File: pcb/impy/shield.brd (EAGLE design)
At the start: 133 x 107 mm, 117 parts, among them J1 USB-2410-06, J2 SI-60062-F, J3 5V, U1 AD5933YRS, U10 LTC3406AB, U11 23LCV1024-I/SN, U12 MIC2009A-1YM6, U13 ADG725BSU, U14 ADG725BSU, U2 ADG704BRM, U3 AD8656ARZ, U4 M24C08WMN, U5 ADG706BRU, U6 DP83848I, U7 MIC2009A-1YM6, U8 AT25DF081A-SS, U9 SST25VF080B-80-4I-S2

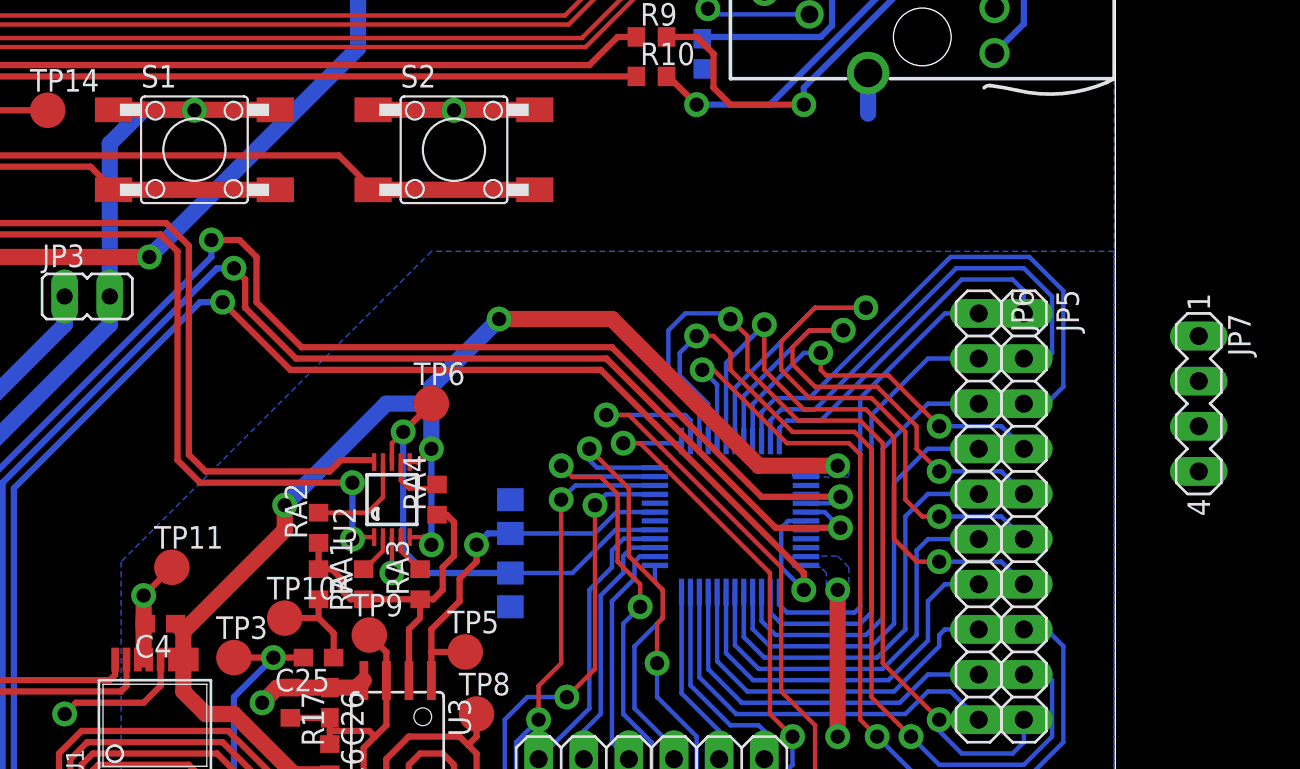
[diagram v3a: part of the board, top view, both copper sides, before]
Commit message: * pcb/impy: (shield.brd) Place and connect I2C header.
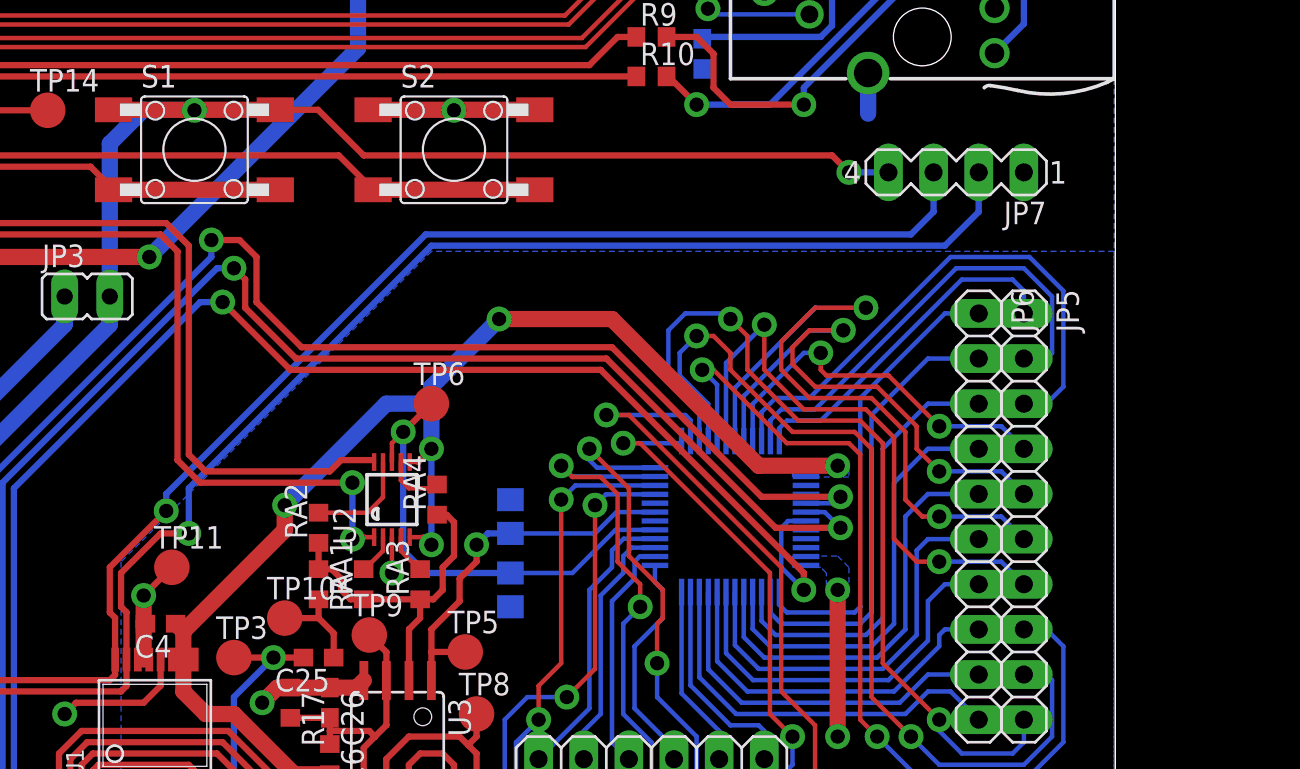
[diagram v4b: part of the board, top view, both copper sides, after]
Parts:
- moved JP7 18.9 mm to (86.0, 74.0), turned to 180 degrees
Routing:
- net PB9: track 27.5 -> 92.9 mm, vias 1 -> 2
- net PB6: track 29.6 -> 92.3 mm, vias 1 -> 2
- net VDD: track 58.3 -> 94.3 mm, vias 1 -> 2
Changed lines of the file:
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@@
 <attribute name="RS" value="737-8791" x="97.155" y="-6.35" size="1.778" layer="27" display="off"/>
 </element>
-<element name="JP7" library="con-lstb" package="MA04-1" value="I2C" x="99.695" y="60.96" rot="R270">
-<attribute name="OC_NEWARK" value="unknown" x="3.175" y="0" size="1.778" layer="27" rot="R270" display="off"/>
-<attribute name="MPN" value="" x="3.175" y="0" size="1.778" layer="27" rot="R270" display="off"/>
-<attribute name="MF" value="" x="3.175" y="0" size="1.778" layer="27" rot="R270" display="off"/>
-<attribute name="OC_FARNELL" value="unknown" x="3.175" y="0" size="1.778" layer="27" rot="R270" display="off"/>
+<element name="JP7" library="con-lstb" package="MA04-1" value="I2C" x="86.0425" y="73.9775" rot="R180">
+<attribute name="OC_NEWARK" value="unknown" x="25.0825" y="170.4975" size="1.778" layer="27" rot="R180" display="off"/>
+<attribute name="MPN" value="" x="25.0825" y="170.4975" size="1.778" layer="27" rot="R180" display="off"/>
+<attribute name="MF" value="" x="25.0825" y="170.4975" size="1.778" layer="27" rot="R180" display="off"/>
+<attribute name="OC_FARNELL" value="unknown" x="25.0825" y="170.4975" size="1.778" layer="27" rot="R180" display="off"/>
 </element>
 <element name="U6" library="parts" package="LQFP48" value="DP83848I" x="-10.795" y="78.105" rot="MR270">
@@
 <contactref element="JP7" pad="4"/>
 <wire x1="30.48" y1="57.4675" x2="38.4175" y2="65.405" width="0.9144" layer="16"/>
-<wire x1="47.73" y1="77.4975" x2="99.695" y2="57.15" width="0" layer="19" extent="1-1"/>
+<wire x1="47.73" y1="77.4975" x2="50.1375" y2="77.4975" width="0.3556" layer="1"/>
+<wire x1="50.1375" y1="77.4975" x2="52.705" y2="74.93" width="0.3556" layer="1"/>
+<wire x1="52.705" y1="74.93" x2="79.0575" y2="74.93" width="0.3556" layer="1"/>
+<wire x1="79.0575" y1="74.93" x2="80.01" y2="73.9775" width="0.3556" layer="1"/>
+<via x="80.01" y="73.9775" extent="1-16" drill="0.8" shape="octagon"/>
+<wire x1="80.01" y1="73.9775" x2="82.2325" y2="73.9775" width="0.3556" layer="16"/>
 <wire x1="-24.13" y1="60.96" x2="30.48" y2="57.4675" width="0" layer="19" extent="16-16"/>
 <wire x1="-26.67" y1="60.96" x2="-24.13" y2="60.96" width="0" layer="19" extent="1-1"/>
@@
 <wire x1="36.5125" y1="44.1325" x2="35.8775" y2="43.4975" width="0.3556" layer="1"/>
 <via x="35.8775" y="43.4975" extent="1-16" drill="0.8" shape="octagon"/>
-<wire x1="81.0895" y1="77.2795" x2="99.695" y2="64.77" width="0" layer="19" extent="16-16"/>
-<wire x1="-26.67" y1="58.42" x2="-26.67" y2="63.5" width="0" layer="19" extent="1-1"/>
-<wire x1="-26.67" y1="35.56" x2="-26.67" y2="58.42" width="0" layer="19" extent="1-1"/>
-<wire x1="-51.7525" y1="41.5325" x2="-26.67" y2="35.56" width="0" layer="19" extent="1-1"/>
-<wire x1="-57.4675" y1="44.5525" x2="-51.7525" y2="41.5325" width="0" layer="19" extent="1-1"/>
-<wire x1="-66.3575" y1="49.1525" x2="-57.4675" y2="44.5525" width="0" layer="19" extent="1-1"/>
-<wire x1="-67.6275" y1="49.1525" x2="-66.3575" y2="49.1525" width="0" layer="19" extent="1-1"/>
+<wire x1="-73.9775" y1="38.9925" x2="-79.6925" y2="41.3775" width="0" layer="19" extent="1-1"/>
+<wire x1="-73.9875" y1="38.4385" x2="-73.9775" y2="38.9925" width="0" layer="19" extent="1-1"/>
+<wire x1="-67.6275" y1="49.1525" x2="-73.9775" y2="38.9925" width="0" layer="19" extent="1-1"/>
+<wire x1="-66.3575" y1="49.1525" x2="-67.6275" y2="49.1525" width="0" layer="19" extent="1-1"/>
 <wire x1="-72.0725" y1="52.1725" x2="-67.6275" y2="49.1525" width="0" layer="19" extent="1-1"/>
 <wire x1="-68.8975" y1="54.3525" x2="-72.0725" y2="52.1725" width="0" layer="19" extent="1-1"/>
-<wire x1="-73.9775" y1="38.9925" x2="-67.6275" y2="49.1525" width="0" layer="19" extent="1-1"/>
-<wire x1="-73.9875" y1="38.4385" x2="-73.9775" y2="38.9925" width="0" layer="19" extent="1-1"/>
-<wire x1="-79.6925" y1="41.3775" x2="-73.9775" y2="38.9925" width="0" layer="19" extent="1-1"/>
+<wire x1="-57.4675" y1="44.5525" x2="-66.3575" y2="49.1525" width="0" layer="19" extent="1-1"/>
+<wire x1="-51.7525" y1="41.5325" x2="-57.4675" y2="44.5525" width="0" layer="19" extent="1-1"/>
 <wire x1="-58.84" y1="31.4325" x2="-51.7525" y2="41.5325" width="0" layer="19" extent="1-1"/>
 <wire x1="-59.175" y1="28.8925" x2="-58.84" y2="31.4325" width="0" layer="19" extent="1-1"/>
+<wire x1="-26.67" y1="35.56" x2="-51.7525" y2="41.5325" width="0" layer="19" extent="1-1"/>
+<wire x1="-26.67" y1="58.42" x2="-26.67" y2="35.56" width="0" layer="19" extent="1-1"/>
+<wire x1="-26.67" y1="63.5" x2="-26.67" y2="58.42" width="0" layer="19" extent="1-1"/>
 </signal>
 <signal name="+5V" class="1">
@@
 <wire x1="27.94" y1="41.91" x2="30.7975" y2="44.7675" width="0.3556" layer="1"/>
 <wire x1="30.7975" y1="44.7675" x2="39.0525" y2="44.7675" width="0.3556" layer="1"/>
-<wire x1="39.3575" y1="46.5625" x2="99.695" y2="62.23" width="0" layer="19" extent="1-1"/>
+<wire x1="39.3575" y1="46.5625" x2="39.3575" y2="49.225" width="0.3556" layer="1"/>
+<wire x1="39.3575" y1="49.225" x2="39.0525" y2="49.53" width="0.3556" layer="1"/>
+<wire x1="39.0525" y1="49.53" x2="39.0525" y2="51.435" width="0.3556" layer="1"/>
+<wire x1="39.0525" y1="51.435" x2="41.275" y2="53.6575" width="0.3556" layer="1"/>
+<wire x1="41.275" y1="53.6575" x2="42.8625" y2="53.6575" width="0.3556" layer="1"/>
+<via x="42.8625" y="53.6575" extent="1-16" drill="0.8" shape="octagon"/>
+<wire x1="42.8625" y1="53.6575" x2="42.8625" y2="56.1975" width="0.3556" layer="16"/>
+<wire x1="42.8625" y1="56.1975" x2="56.515" y2="69.85" width="0.3556" layer="16"/>
+<wire x1="56.515" y1="69.85" x2="85.4075" y2="69.85" width="0.3556" layer="16"/>
+<wire x1="85.4075" y1="69.85" x2="87.3125" y2="71.755" width="0.3556" layer="16"/>
+<wire x1="87.3125" y1="71.755" x2="87.3125" y2="73.9775" width="0.3556" layer="16"/>
 <wire x1="-66.3575" y1="54.3525" x2="21.9075" y2="40.9575" width="0" layer="19" extent="1-1"/>
 </signal>
@@
 <wire x1="20.6375" y1="41.91" x2="20.6375" y2="36.83" width="0.3556" layer="1"/>
 <wire x1="20.6375" y1="36.83" x2="21.9075" y2="35.56" width="0.3556" layer="1"/>
-<wire x1="38.7175" y1="46.5625" x2="99.695" y2="59.69" width="0" layer="19" extent="1-1"/>
+<wire x1="38.7175" y1="46.5625" x2="38.7175" y2="48.9125" width="0.3556" layer="1"/>
+<wire x1="38.7175" y1="48.9125" x2="38.4175" y2="49.2125" width="0.3556" layer="1"/>
+<wire x1="38.4175" y1="49.2125" x2="38.4175" y2="51.7525" width="0.3556" layer="1"/>
+<wire x1="38.4175" y1="51.7525" x2="41.5925" y2="54.9275" width="0.3556" layer="1"/>
+<via x="41.5925" y="54.9275" extent="1-16" drill="0.8" shape="octagon"/>
+<wire x1="41.5925" y1="54.9275" x2="41.5925" y2="55.88" width="0.3556" layer="16"/>
+<wire x1="41.5925" y1="55.88" x2="56.1975" y2="70.485" width="0.3556" layer="16"/>
+<wire x1="56.1975" y1="70.485" x2="83.5025" y2="70.485" width="0.3556" layer="16"/>
+<wire x1="83.5025" y1="70.485" x2="84.7725" y2="71.755" width="0.3556" layer="16"/>
+<wire x1="84.7725" y1="71.755" x2="84.7725" y2="73.9775" width="0.3556" layer="16"/>
 <wire x1="-67.6275" y1="54.3525" x2="20.6375" y2="41.91" width="0" layer="19" extent="1-1"/>
 </signal>

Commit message: * pcb/impy: (shield.sch) Fix missing ground connection on discovery connector.
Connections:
- net GND: now also JP2.49
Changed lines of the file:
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@@
 <wire x1="36.5125" y1="44.1325" x2="35.8775" y2="43.4975" width="0.3556" layer="1"/>
 <via x="35.8775" y="43.4975" extent="1-16" drill="0.8" shape="octagon"/>
+<contactref element="JP2" pad="49"/>
 <wire x1="-73.9775" y1="38.9925" x2="-79.6925" y2="41.3775" width="0" layer="19" extent="1-1"/>
 <wire x1="-73.9875" y1="38.4385" x2="-73.9775" y2="38.9925" width="0" layer="19" extent="1-1"/>

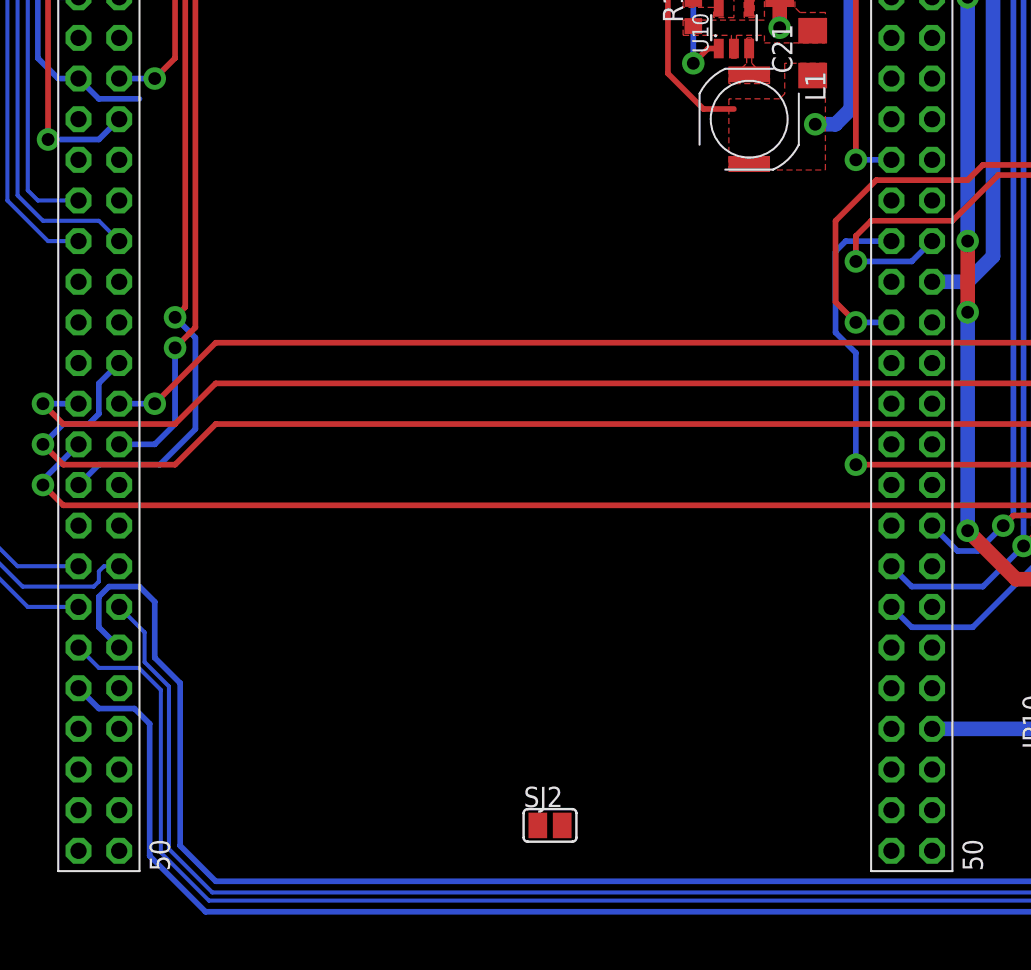
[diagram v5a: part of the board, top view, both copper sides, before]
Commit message: * pcb/impy: (shield.brd) Place and route ETH_CLK solder jumper.
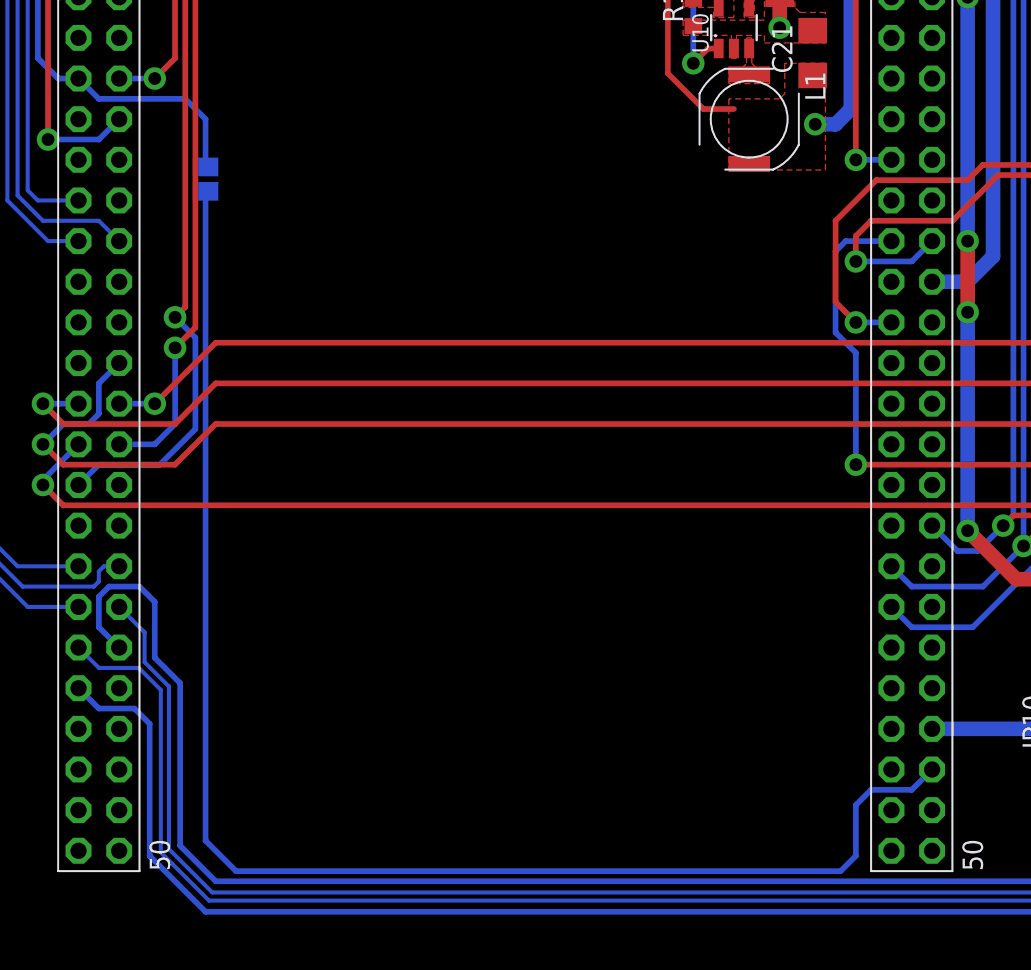
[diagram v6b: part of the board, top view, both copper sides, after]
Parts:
- moved SJ2 45.8 mm to (-18.7, 44.5), flipped to the bottom, turned to 270 degrees
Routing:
- net PC9: track 0.00 -> 91.3 mm
- net ETH_CLK: track 46.2 -> 53.9 mm
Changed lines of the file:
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@@
 <element name="C23" library="rcl" package="C0603" value="100n" x="-10.95375" y="69.5325" rot="MR270"/>
 <element name="R11" library="rcl" package="R0603" value="2k2" x="-13.0175" y="69.5325" rot="MR270"/>
-<element name="SJ2" library="jumper" package="SJ" value="ETH_CLK" x="2.794" y="4.1275"/>
+<element name="SJ2" library="jumper" package="SJ" value="ETH_CLK" x="-18.7325" y="44.5135" rot="MR270"/>
 <element name="S2" library="parts" package="FSM" value="FSM4JSMATR" x="57.785" y="75.2475" rot="R270">
 <attribute name="RS" value="718-2455" x="28.575" y="56.1975" size="1.778" layer="27" rot="R270" display="off"/>
@@
 <wire x1="-28.575" y1="68.58" x2="-29.21" y2="67.945" width="0.3556" layer="16"/>
 <wire x1="-26.67" y1="50.8" x2="-25.4" y2="49.53" width="0.3556" layer="16"/>
-<wire x1="-25.4" y1="49.53" x2="-22.86" y2="49.53" width="0.3556" layer="16"/>
 <wire x1="-29.21" y1="52.07" x2="-27.94" y2="50.8" width="0.3556" layer="16"/>
 <wire x1="-27.94" y1="50.8" x2="-26.67" y2="50.8" width="0.3556" layer="16"/>
-<wire x1="2.032" y1="4.1275" x2="-22.86" y2="49.53" width="0" layer="19" extent="1-16"/>
+<wire x1="-25.4" y1="49.53" x2="-20.0025" y2="49.53" width="0.3556" layer="16"/>
+<wire x1="-20.0025" y1="49.53" x2="-18.7325" y2="48.26" width="0.3556" layer="16"/>
+<wire x1="-18.7325" y1="48.26" x2="-18.7325" y2="45.2755" width="0.3556" layer="16"/>
 </signal>
 <signal name="PC12">
@@
 <contactref element="JP2" pad="46"/>
 <contactref element="SJ2" pad="2"/>
-<wire x1="3.556" y1="4.1275" x2="26.67" y2="7.62" width="0" layer="19" extent="1-1"/>
+<wire x1="26.67" y1="7.62" x2="25.4" y2="6.35" width="0.3556" layer="16"/>
+<wire x1="25.4" y1="6.35" x2="22.86" y2="6.35" width="0.3556" layer="16"/>
+<wire x1="22.86" y1="6.35" x2="21.9075" y2="5.3975" width="0.3556" layer="16"/>
+<wire x1="21.9075" y1="5.3975" x2="21.9075" y2="2.2225" width="0.3556" layer="16"/>
+<wire x1="21.9075" y1="2.2225" x2="20.955" y2="1.27" width="0.3556" layer="16"/>
+<wire x1="20.955" y1="1.27" x2="-16.8275" y2="1.27" width="0.3556" layer="16"/>
+<wire x1="-16.8275" y1="1.27" x2="-18.7325" y2="3.175" width="0.3556" layer="16"/>
+<wire x1="-18.7325" y1="3.175" x2="-18.7325" y2="43.7515" width="0.3556" layer="16"/>
 </signal>
 <signal name="N$20">
